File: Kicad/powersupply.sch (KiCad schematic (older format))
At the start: 37 parts, among them J901 Jack-DC, J902 Double-mini-DIN-6, Q901 BC548, SW901 SW_DIP_x01, SW902 SW_DIP_x01, U901 5V DC-DC Module, U902 TLV1117 3.3V 1A, U903 MAX1615, U904 STM32F030F4Px

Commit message: Switch to 8 pin debug header (J902)
Closes #15
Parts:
- removed JP901: Jumper, Connector_PinHeader_2.54mm:PinHeader_1x02_P2.54mm_Vertical, symbol Device:Jumper_NO_Small
- removed JP902, JP903: Jumper, Connector_PinHeader_2.54mm:PinHeader_1x02_P2.54mm_Vertical, symbol Device:Jumper_NC_Small
- removed TP902, TP903: TestPoint, Connector_PinHeader_2.54mm:PinHeader_1x01_P2.54mm_Vertical, symbol Connector:TestPoint
- added J902: Conn_02x04_Odd_Even, Connector_PinHeader_2.54mm:PinHeader_2x04_P2.54mm_Vertical, symbol Connector_Generic:Conn_02x04_Odd_Even
- renumbered J902 to J903, R905 to R902, R907 to R903, R909 to R904, R903 to R905, R902 to R906, R904 to R907, R906 to R908, R908 to R909
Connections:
- wire segments 166 -> 162
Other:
- note added: "Normal Operation:\n* Remove all connections from J902\n* Fit jumper to J902 1-2\n* Fit jumper to J902 3-4\n\nUART Programming:\n* Remove all connections from J902\n* Fit jumper to Jx 5-7 to select Bootloader\n* Connect J902 Pin 2 to UART RX\n* Connect J902 Pin 4 to UART TX\n* Connect DC power\n* Short J902 6-8 to reset BMC as required\n"
- note removed: "UART Programming:\n* Fit jumper to JP901\n* Remove jumper from J902 and J903\n* Connect J902 Pin 1 to UART RX\n* Connect J903 Pin 1 to UART TX\n* Connect DC power"
- moved on the sheet: R907

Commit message: K7805-3AR3 updates:
) Add footprint with courtyard.
) Note that several of the pins are duplicated, not independent.
) Add aliases for other voltage variants.
) Tidy up schematic back on to the 50 mil grid.
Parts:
- U901: symbol Neotron-Common-Hardware:K78xx-3AR3 -> Neotron-Common-Hardware:K78(L)05-3AR3; Manufacturer Mornsun America, LLC -> Mornsun
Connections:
- wire segments 162 -> 143
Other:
- note added: "This small PSU runs our\nboard management controller"
- note removed: "This small PSU runs our\nboard management MCU"
- moved on the sheet: C901, C902, C903, C904, C905, C906, C907, F901, J901, L901, U902, U903

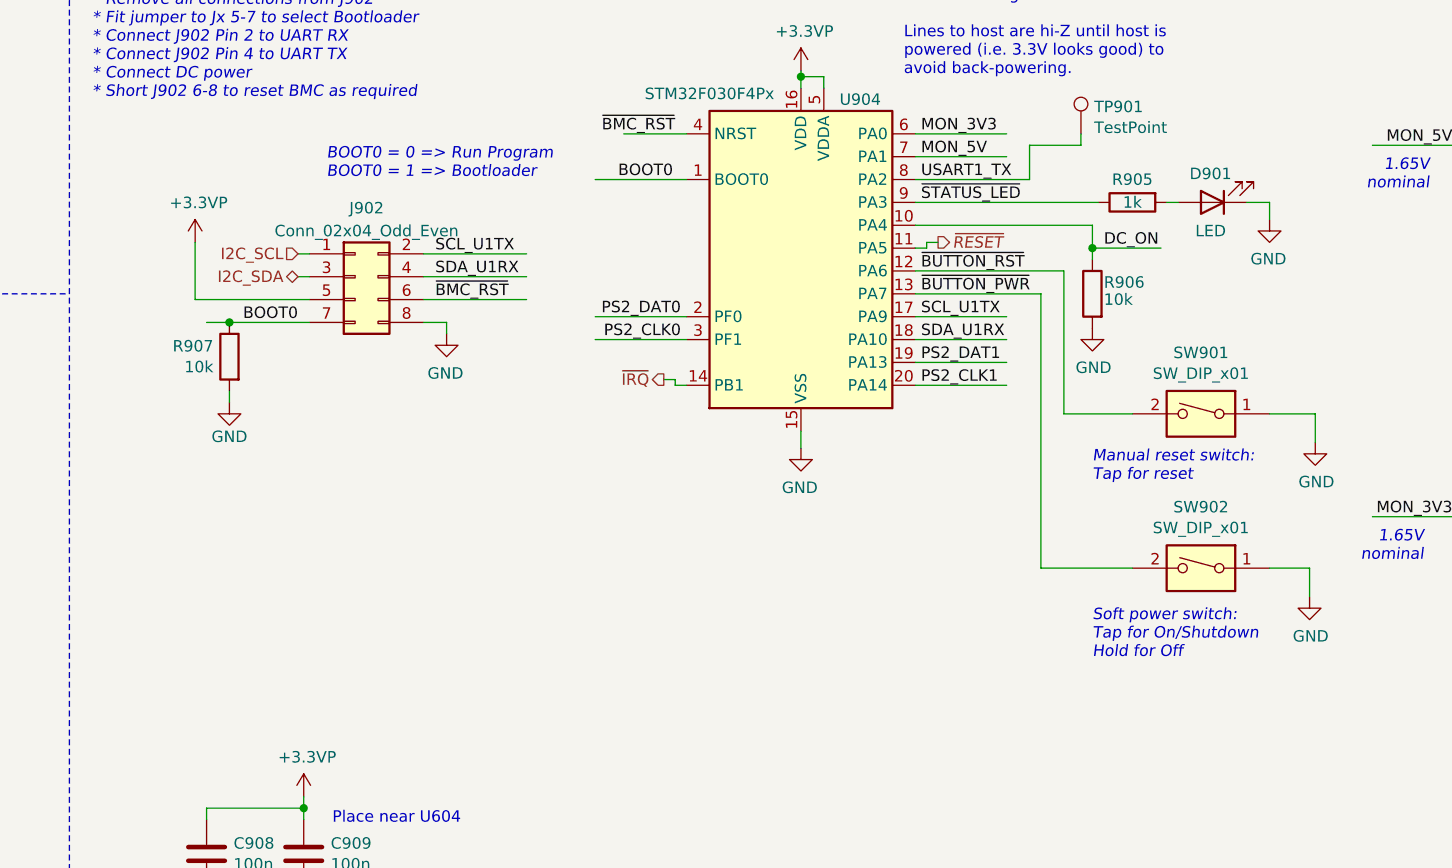
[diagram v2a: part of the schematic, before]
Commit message: Add 2.54mm header for case LED.
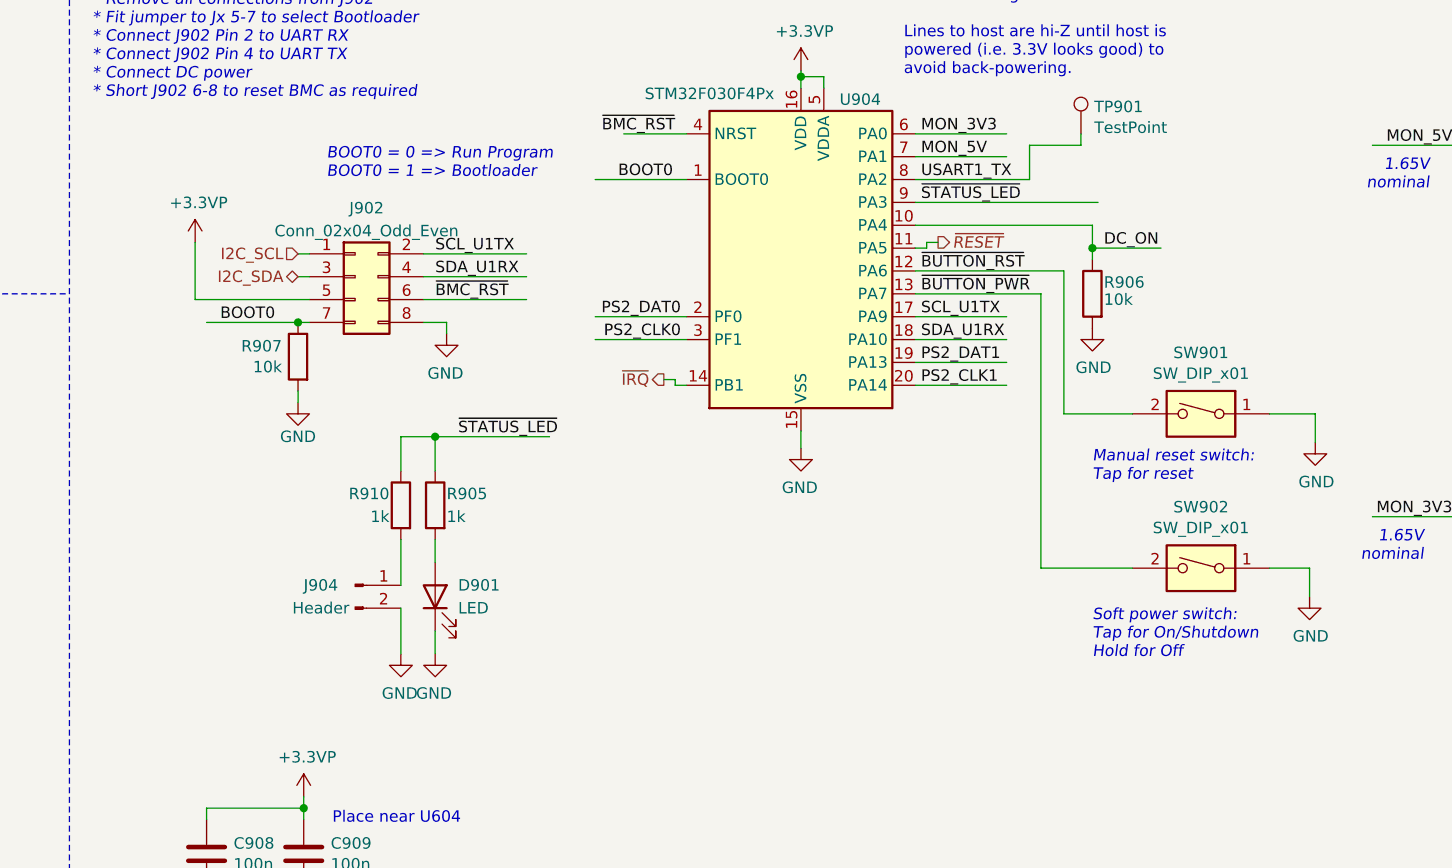
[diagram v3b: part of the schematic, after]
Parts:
- added J904: Header, Connector_PinHeader_2.54mm:PinHeader_1x02_P2.54mm_Vertical, symbol Connector:Conn_01x02_Male
- added R910: 1k, Resistor_SMD:R_0805_2012Metric_Pad1.15x1.40mm_HandSolder, symbol Device:R
- J902: DNP (none) -> 1
- Q901: Digikey (none) -> BC548BU-ND; MPN (none) -> BC548BU; Manufacturer (none) -> ON Semi
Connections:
- wire segments 143 -> 148
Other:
- moved on the sheet: D901, R905, R907
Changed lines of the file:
@@
 DC_ON
-$Comp
-L Device:LED D901
-U 1 1 5FF7ECF6
-P 9700 4175
-F 0 "D901" H 9800 4050 50  0000 R CNN
-F 1 "LED" H 9775 4300 50  0000 R CNN
-F 2 "LED_THT:LED_D3.0mm" H 9700 4175 50  0001 C CNN
-F 3 "~" H 9700 4175 50  0001 C CNN
-F 4 "0" H 9700 4175 50  0001 C CNN "DNP"
-F 5 "732-5006-ND" H 9700 4175 50  0001 C CNN "Digikey"
-F 6 "151031SS06000" H 9700 4175 50  0001 C CNN "MPN"
-F 7 "Würth" H 9700 4175 50  0001 C CNN "Manufacturer"
-	1    9700 4175
-	-1   0    0    1
-$EndComp
 $Comp
 L power:GND #PWR0916
 U 1 1 5FF7ED00
-P 9950 4250
-F 0 "#PWR0916" H 9950 4000 50  0001 C CNN
-F 1 "GND" H 9955 4077 50  0000 C CNN
-F 2 "" H 9950 4250 50  0001 C CNN
-F 3 "" H 9950 4250 50  0001 C CNN
-	1    9950 4250
+P 6300 6150
+F 0 "#PWR0916" H 6300 5900 50  0001 C CNN
+F 1 "GND" H 6305 5977 50  0000 C CNN
+F 2 "" H 6300 6150 50  0001 C CNN
+F 3 "" H 6300 6150 50  0001 C CNN
+	1    6300 6150
 	-1   0    0    -1
 $EndComp
@@
 L Device:R R905
 U 1 1 5FF7ED0A
-P 9350 4175
-F 0 "R905" V 9250 4175 50  0000 C CNN
-F 1 "1k" V 9350 4175 50  0000 C CNN
-F 2 "Resistor_SMD:R_0805_2012Metric_Pad1.15x1.40mm_HandSolder" V 9280 4175 50  0001 C CNN
-F 3 "~" H 9350 4175 50  0001 C CNN
-F 4 "0" H 9350 4175 50  0001 C CNN "DNP"
-F 5 "RMCF0805FT1K00-ND" H 9350 4175 50  0001 C CNN "Digikey"
-F 6 "RMCF0805FT1K00" H 9350 4175 50  0001 C CNN "MPN"
-F 7 "Stackpole" H 9350 4175 50  0001 C CNN "Manufacturer"
-	1    9350 4175
-	0    -1   1    0
-$EndComp
-Wire Wire Line
-	9950 4175 9950 4250
-Wire Wire Line
-	9500 4175 9550 4175
+P 6300 5500
+F 0 "R905" H 6250 5550 50  0000 R CNN
+F 1 "1k" H 6250 5450 50  0000 R CNN
+F 2 "Resistor_SMD:R_0805_2012Metric_Pad1.15x1.40mm_HandSolder" V 6230 5500 50  0001 C CNN
+F 3 "~" H 6300 5500 50  0001 C CNN
+F 4 "0" H 6300 5500 50  0001 C CNN "DNP"
+F 5 "RMCF0805FT1K00-ND" H 6300 5500 50  0001 C CNN "Digikey"
+F 6 "RMCF0805FT1K00" H 6300 5500 50  0001 C CNN "MPN"
+F 7 "Stackpole" H 6300 5500 50  0001 C CNN "Manufacturer"
+	1    6300 5500
+	-1   0    0    -1
+$EndComp
 Text HLabel 8500 4350 2    50   Output Italic 0
 ~RESET
@@
 F 3 "http://www.fairchildsemi.com/ds/BC/BC547.pdf" H 1700 2600 50  0001 L CNN
 F 4 "0" H 1700 2600 50  0001 C CNN "DNP"
+F 5 "BC548BU-ND" H 1700 2600 50  0001 C CNN "Digikey"
+F 6 "BC548BU" H 1700 2600 50  0001 C CNN "MPN"
+F 7 "ON Semi" H 1700 2600 50  0001 C CNN "Manufacturer"
 	1    1700 2600
 	1    0    0    -1
@@
 $EndComp
 Wire Wire Line
-	9850 4175 9950 4175
-Wire Wire Line
 	9175 4275 9175 4375
 Wire Wire Line
@@
 L Device:R R907
 U 1 1 6017DAF5
-P 5400 4850
-F 0 "R907" H 5470 4896 50  0000 L CNN
-F 1 "10k" H 5470 4805 50  0000 L CNN
-F 2 "Resistor_SMD:R_0805_2012Metric_Pad1.15x1.40mm_HandSolder" V 5330 4850 50  0001 C CNN
-F 3 "~" H 5400 4850 50  0001 C CNN
-F 4 "0" H 5400 4850 50  0001 C CNN "DNP"
-F 5 "RMCF0805FT10K0-ND" H 5400 4850 50  0001 C CNN "Digikey"
-F 6 "RMCF0805FT10K0" H 5400 4850 50  0001 C CNN "MPN"
-F 7 "Stackpole" H 5400 4850 50  0001 C CNN "Manufacturer"
-	1    5400 4850
+P 5700 4850
+F 0 "R907" H 5770 4896 50  0000 L CNN
+F 1 "10k" H 5770 4805 50  0000 L CNN
+F 2 "Resistor_SMD:R_0805_2012Metric_Pad1.15x1.40mm_HandSolder" V 5630 4850 50  0001 C CNN
+F 3 "~" H 5700 4850 50  0001 C CNN
+F 4 "0" H 5700 4850 50  0001 C CNN "DNP"
+F 5 "RMCF0805FT10K0-ND" H 5700 4850 50  0001 C CNN "Digikey"
+F 6 "RMCF0805FT10K0" H 5700 4850 50  0001 C CNN "MPN"
+F 7 "Stackpole" H 5700 4850 50  0001 C CNN "Manufacturer"
+	1    5700 4850
 	-1   0    0    -1
 $EndComp
@@
 F 2 "Connector_PinHeader_2.54mm:PinHeader_2x04_P2.54mm_Vertical" H 5950 4500 50  0001 C CNN
 F 3 "~" H 5950 4500 50  0001 C CNN
+F 4 "1" H 5950 4500 50  0001 C CNN "DNP"
+F 5 "~" H 5950 4500 50  0001 C CNN "Digikey"
+F 6 "~" H 5950 4500 50  0001 C CNN "MPN"
+F 7 "~" H 5950 4500 50  0001 C CNN "Manufacturer"
 	1    5950 4500
 	1    0    0    -1
@@
 Wire Wire Line
 	6250 4400 6700 4400
-Text Label 5700 4700 2    50   ~ 0
+Text Label 5600 4700 2    50   ~ 0
 BOOT0
 Wire Wire Line
-	5750 4700 5400 4700
+	5750 4700 5700 4700
 Wire Wire Line
 	5750 4600 5250 4600
 Wire Wire Line
 	5250 4350 5250 4600
-Connection ~ 5400 4700
-Wire Wire Line
-	5400 4700 5300 4700
 $Comp
 L power:GND #PWR0921
 U 1 1 6018389F
-P 5400 5050
-F 0 "#PWR0921" H 5400 4800 50  0001 C CNN
-F 1 "GND" H 5400 4900 50  0000 C CNN
-F 2 "" H 5400 5050 50  0001 C CNN
-F 3 "" H 5400 5050 50  0001 C CNN
-	1    5400 5050
-	1    0    0    -1
-$EndComp
-Wire Wire Line
-	5400 5000 5400 5050
+P 5700 5050
+F 0 "#PWR0921" H 5700 4800 50  0001 C CNN
+F 1 "GND" H 5700 4900 50  0000 C CNN
+F 2 "" H 5700 5050 50  0001 C CNN
+F 3 "" H 5700 5050 50  0001 C CNN
+	1    5700 5050
+	1    0    0    -1
+$EndComp
+Wire Wire Line
+	5700 5000 5700 5050
 Wire Wire Line
 	6250 4700 6350 4700
@@
 Wire Wire Line
 	4500 1400 5500 1400
+$Comp
+L Device:LED D901
+U 1 1 5FF7ECF6
+P 6300 5900
+F 0 "D901" V 6350 5800 50  0000 R CNN
+F 1 "LED" V 6250 5800 50  0000 R CNN
+F 2 "LED_THT:LED_D3.0mm" H 6300 5900 50  0001 C CNN
+F 3 "~" H 6300 5900 50  0001 C CNN
+F 4 "0" H 6300 5900 50  0001 C CNN "DNP"
+F 5 "732-5006-ND" H 6300 5900 50  0001 C CNN "Digikey"
+F 6 "151031SS06000" H 6300 5900 50  0001 C CNN "MPN"
+F 7 "Würth" H 6300 5900 50  0001 C CNN "Manufacturer"
+	1    6300 5900
+	0    -1   -1   0
+$EndComp
+Text Label 6400 5200 0    50   ~ 0
+~STATUS_LED
+Wire Wire Line
+	6300 6150 6300 6050
+Wire Wire Line
+	6300 5650 6300 5750
+$Comp
+L power:GND #PWR0932
+U 1 1 6020C50C
+P 6150 6150
+F 0 "#PWR0932" H 6150 5900 50  0001 C CNN
+F 1 "GND" H 6155 5977 50  0000 C CNN
+F 2 "" H 6150 6150 50  0001 C CNN
+F 3 "" H 6150 6150 50  0001 C CNN
+	1    6150 6150
+	-1   0    0    -1
+$EndComp
+$Comp
+L Device:R R910
+U 1 1 6020C51A
+P 6150 5500
+F 0 "R910" H 6200 5550 50  0000 L CNN
+F 1 "1k" H 6200 5450 50  0000 L CNN
+F 2 "Resistor_SMD:R_0805_2012Metric_Pad1.15x1.40mm_HandSolder" V 6080 5500 50  0001 C CNN
+F 3 "~" H 6150 5500 50  0001 C CNN
+F 4 "0" H 6150 5500 50  0001 C CNN "DNP"
+F 5 "RMCF0805FT1K00-ND" H 6150 5500 50  0001 C CNN "Digikey"
+F 6 "RMCF0805FT1K00" H 6150 5500 50  0001 C CNN "MPN"
+F 7 "Stackpole" H 6150 5500 50  0001 C CNN "Manufacturer"
+	1    6150 5500
+	-1   0    0    -1
+$EndComp
+$Comp
+L Connector:Conn_01x02_Male J904
+U 1 1 60214012
+P 5950 5850
+F 0 "J904" H 5800 5850 50  0000 C CNN
+F 1 "Header" H 5800 5750 50  0000 C CNN
+F 2 "Connector_PinHeader_2.54mm:PinHeader_1x02_P2.54mm_Vertical" H 5950 5850 50  0001 C CNN
+F 3 "~" H 5950 5850 50  0001 C CNN
+F 4 "1" H 5950 5850 50  0001 C CNN "DNP"
+F 5 "~" H 5950 5850 50  0001 C CNN "Digikey"
+F 6 "~" H 5950 5850 50  0001 C CNN "MPN"
+F 7 "~" H 5950 5850 50  0001 C CNN "Manufacturer"
+	1    5950 5850
+	1    0    0    -1
+$EndComp
+Wire Wire Line
+	6150 5950 6150 6150
+Wire Wire Line
+	6150 5650 6150 5850
+Wire Wire Line
+	6800 5200 6300 5200
+Wire Wire Line
+	6300 5350 6300 5200
+Wire Wire Line
+	6300 5200 6150 5200
+Wire Wire Line
+	6150 5200 6150 5350
+Connection ~ 6300 5200
+Connection ~ 5700 4700
+Wire Wire Line
+	5300 4700 5700 4700
 $EndSCHEMATC
